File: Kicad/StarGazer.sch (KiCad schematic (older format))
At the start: 5 parts, among them U1 STM32F070F6Px

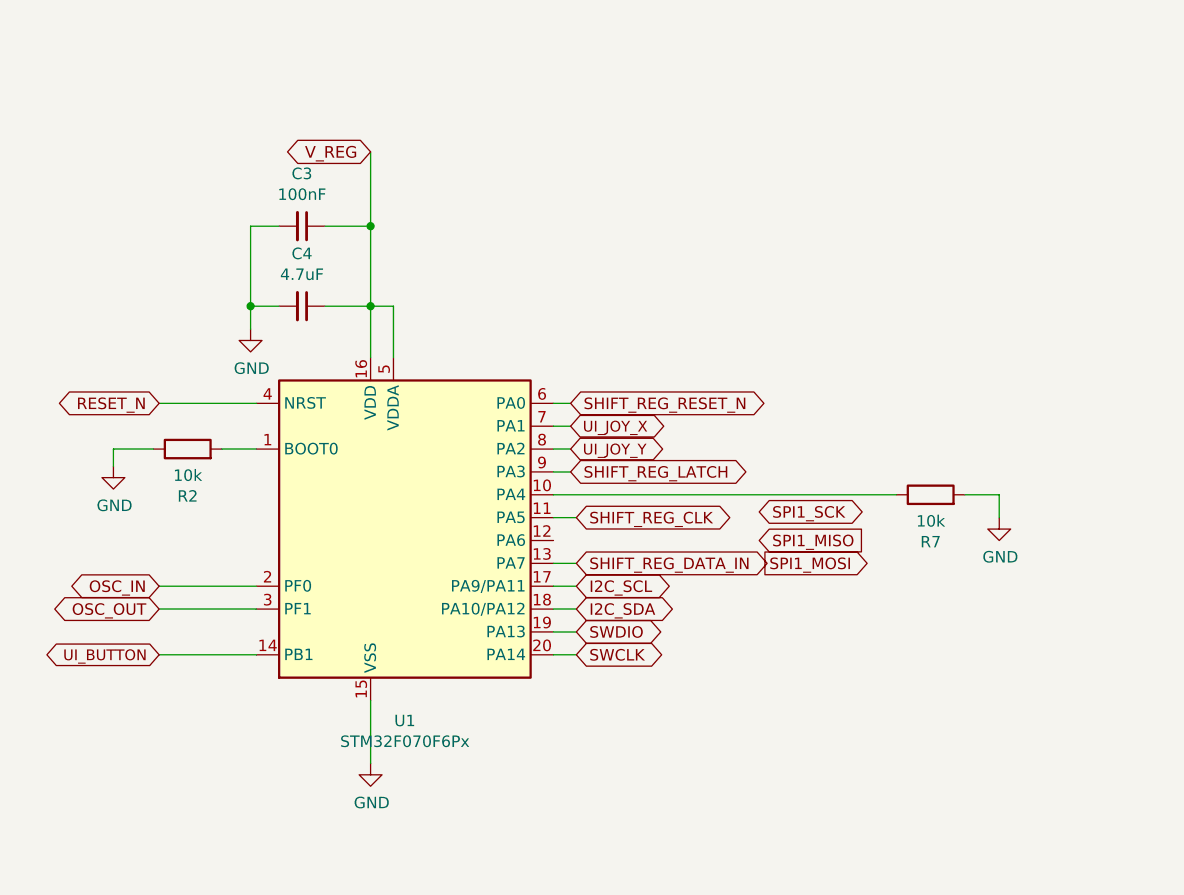
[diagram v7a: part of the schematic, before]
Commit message: Assigned footprints to majority of refs. Missing is i2c due to unknown trace length.
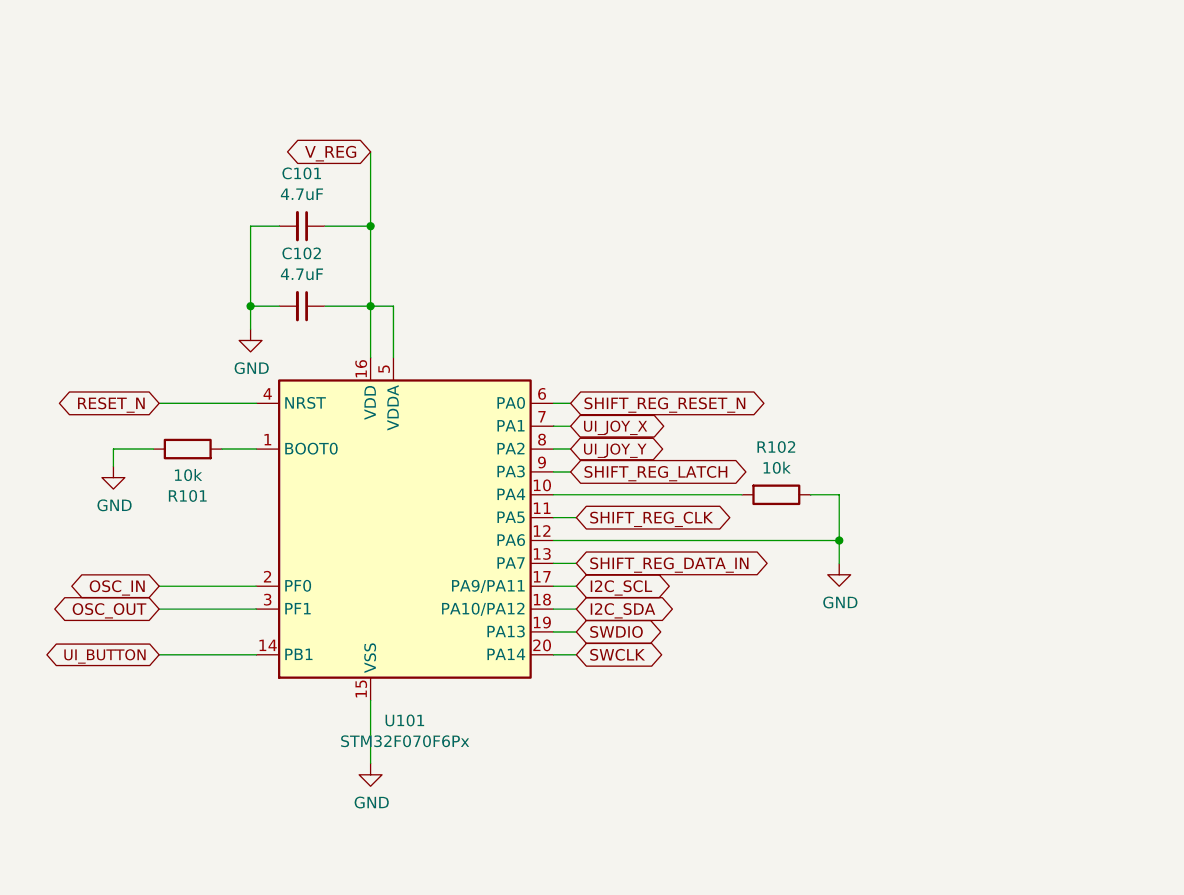
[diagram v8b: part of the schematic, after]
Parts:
- C101: renamed from C3; value 100nF -> 4.7uF; footprint (none) -> Capacitor_SMD:C_0805_2012Metric_Pad1.15x1.40mm_HandSolder; part_name (none) -> Capactitor - Bypass; part_url (none) -> https://www.digikey.com/product-detail/en/w%C3%BCrth-elektr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
- C102: renamed from C4; footprint (none) -> Capacitor_SMD:C_0805_2012Metric_Pad1.15x1.40mm_HandSolder; part_name (none) -> Capactitor - Bypass; part_url (none) -> https://www.digikey.com/product-detail/en/w%C3%BCrth-elektr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
- renumbered R2 to R101, R7 to R102, U1 to U101
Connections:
- net GND: now also R102.1, U101.12 (PA6); no longer R102.2
- net at U101.10 (PA4): now also R102.2; no longer R102.1
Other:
- moved on the sheet: R102
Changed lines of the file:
@@
 OSC_OUT
 $Comp
-L power:GND #PWR0101
+L power:GND #PWR0103
 U 1 1 5F3EE3F5
 P 5300 4850
-F 0 "#PWR0101" H 5300 4600 50  0001 C CNN
+F 0 "#PWR0103" H 5300 4600 50  0001 C CNN
 F 1 "GND" H 5305 4677 50  0000 C CNN
 F 2 "" H 5300 4850 50  0001 C CNN
@@
 RESET_N
 $Comp
-L MCU_ST_STM32F0:STM32F070F6Px U1
+L MCU_ST_STM32F0:STM32F070F6Px U101
 U 1 1 5F3ECB3C
 P 5500 3775
-F 0 "U1" H 5450 2886 50  0000 C CNN
+F 0 "U101" H 5450 2886 50  0000 C CNN
 F 1 "STM32F070F6Px" H 5450 2795 50  0000 C CNN
 F 2 "Package_SO:TSSOP-20_4.4x6.5mm_P0.65mm" H 4900 3075 50  0001 R CNN
@@
 	4650 3475 4800 3475
 $Comp
-L Device:R R2
+L Device:R R101
 U 1 1 5F3FCFD6
 P 4500 3475
-F 0 "R2" V 4293 3475 50  0000 C CNN
+F 0 "R101" V 4293 3475 50  0000 C CNN
 F 1 "10k" V 4384 3475 50  0000 C CNN
 F 2 "Resistor_SMD:R_1206_3216Metric_Pad1.42x1.75mm_HandSolder" V 4430 3475 50  0001 C CNN
@@
 	4175 3475 4175 3550
 $Comp
-L power:GND #PWR0112
+L power:GND #PWR0101
 U 1 1 5F3FD5C8
 P 4175 3550
-F 0 "#PWR0112" H 4175 3300 50  0001 C CNN
+F 0 "#PWR0101" H 4175 3300 50  0001 C CNN
 F 1 "GND" H 4180 3377 50  0000 C CNN
 F 2 "" H 4175 3550 50  0001 C CNN
@@
 V_REG
 $Comp
-L Device:C_Small C3
+L Device:C_Small C101
 U 1 1 5F4EAC14
 P 5000 2500
-F 0 "C3" V 4771 2500 50  0000 C CNN
-F 1 "100nF" V 4862 2500 50  0000 C CNN
-F 2 "" H 5000 2500 50  0001 C CNN
+F 0 "C101" V 4771 2500 50  0000 C CNN
+F 1 "4.7uF" V 4862 2500 50  0000 C CNN
+F 2 "Capacitor_SMD:C_0805_2012Metric_Pad1.15x1.40mm_HandSolder" H 5000 2500 50  0001 C CNN
 F 3 "~" H 5000 2500 50  0001 C CNN
 F 4 "" V 5000 2500 50  0001 C CNN "TestField"
+F 5 "https://www.digikey.com/product-detail/en/w%C3%BCrth-elektronik/885012107009/732-7619-1-ND/5454246" H 5000 2500 50  0001 C CNN "part_url"
+F 6 "Capactitor - Bypass" H 5000 2500 50  0001 C CNN "part_name"
 	1    5000 2500
 	0    1    1    0
 $EndComp
 $Comp
-L Device:C_Small C4
+L Device:C_Small C102
 U 1 1 5F4EB59B
 P 5000 2850
-F 0 "C4" V 4771 2850 50  0000 C CNN
+F 0 "C102" V 4771 2850 50  0000 C CNN
 F 1 "4.7uF" V 4862 2850 50  0000 C CNN
-F 2 "" H 5000 2850 50  0001 C CNN
+F 2 "Capacitor_SMD:C_0805_2012Metric_Pad1.15x1.40mm_HandSolder" H 5000 2850 50  0001 C CNN
 F 3 "~" H 5000 2850 50  0001 C CNN
+F 4 "https://www.digikey.com/product-detail/en/w%C3%BCrth-elektronik/885012107009/732-7619-1-ND/5454246" H 5000 2850 50  0001 C CNN "part_url"
+F 5 "Capactitor - Bypass" H 5000 2850 50  0001 C CNN "part_name"
 	1    5000 2850
 	0    1    1    0
@@
 	4775 2850 4775 2950
 $Comp
-L power:GND #PWR0113
+L power:GND #PWR0102
 U 1 1 5F4F9B1C
 P 4775 2950
-F 0 "#PWR0113" H 4775 2700 50  0001 C CNN
+F 0 "#PWR0102" H 4775 2700 50  0001 C CNN
 F 1 "GND" H 4780 2777 50  0000 C CNN
 F 2 "" H 4775 2950 50  0001 C CNN
@@
 SHIFT_REG_LATCH
 $Comp
-L power:GND #PWR0114
+L power:GND #PWR0104
 U 1 1 5F5511AD
-P 8050 3775
-F 0 "#PWR0114" H 8050 3525 50  0001 C CNN
-F 1 "GND" H 8055 3602 50  0000 C CNN
-F 2 "" H 8050 3775 50  0001 C CNN
-F 3 "" H 8050 3775 50  0001 C CNN
-	1    8050 3775
-	1    0    0    -1
-$EndComp
-Wire Wire Line
-	8050 3775 8050 3675
+P 7350 3975
+F 0 "#PWR0104" H 7350 3725 50  0001 C CNN
+F 1 "GND" H 7355 3802 50  0000 C CNN
+F 2 "" H 7350 3975 50  0001 C CNN
+F 3 "" H 7350 3975 50  0001 C CNN
+	1    7350 3975
+	1    0    0    -1
+$EndComp
+Wire Wire Line
+	7350 3975 7350 3875
 Wire Wire Line
 	6100 3775 6200 3775
-Text GLabel 7000 3750 2    50   BiDi ~ 0
-SPI1_SCK
 Text GLabel 6200 3775 2    50   BiDi ~ 0
 SHIFT_REG_CLK
 Text GLabel 6200 3975 2    50   BiDi ~ 0
 SHIFT_REG_DATA_IN
-Text GLabel 7025 3975 2    50   Output ~ 0
-SPI1_MOSI
-Text GLabel 7000 3875 2    50   Input ~ 0
-SPI1_MISO
-Wire Wire Line
-	8050 3675 7900 3675
-Wire Wire Line
-	7600 3675 6100 3675
-$Comp
-L Device:R R7
+Wire Wire Line
+	7350 3675 7225 3675
+Wire Wire Line
+	6925 3675 6100 3675
+$Comp
+L Device:R R102
 U 1 1 5F54B516
-P 7750 3675
-F 0 "R7" V 7543 3675 50  0000 C CNN
-F 1 "10k" V 7634 3675 50  0000 C CNN
-F 2 "Resistor_SMD:R_1206_3216Metric_Pad1.42x1.75mm_HandSolder" V 7680 3675 50  0001 C CNN
-F 3 "~" H 7750 3675 50  0001 C CNN
-F 4 "" H 7750 3675 50  0001 C CNN "Name"
-F 5 "" H 7750 3675 50  0001 C CNN "part_details"
-F 6 "Resistor - Pull Up" H 7750 3675 50  0001 C CNN "part_name"
-F 7 "https://www.digikey.com/product-detail/en/yageo/RC1206JR-0710KL/311-10KERCT-ND/732156" H 7750 3675 50  0001 C CNN "part_url"
-	1    7750 3675
-	0    -1   -1   0
+P 7075 3675
+F 0 "R102" V 6868 3675 50  0000 C CNN
+F 1 "10k" V 6959 3675 50  0000 C CNN
+F 2 "Resistor_SMD:R_1206_3216Metric_Pad1.42x1.75mm_HandSolder" V 7005 3675 50  0001 C CNN
+F 3 "~" H 7075 3675 50  0001 C CNN
+F 4 "" H 7075 3675 50  0001 C CNN "Name"
+F 5 "" H 7075 3675 50  0001 C CNN "part_details"
+F 6 "Resistor - Pull Up" H 7075 3675 50  0001 C CNN "part_name"
+F 7 "https://www.digikey.com/product-detail/en/yageo/RC1206JR-0710KL/311-10KERCT-ND/732156" H 7075 3675 50  0001 C CNN "part_url"
+	1    7075 3675
+	0    1    1    0
 $EndComp
 Wire Wire Line
@@
 Wire Wire Line
 	6100 3275 6175 3275
+Wire Wire Line
+	6100 3875 7350 3875
+Connection ~ 7350 3875
+Wire Wire Line
+	7350 3875 7350 3675
 $EndSCHEMATC
